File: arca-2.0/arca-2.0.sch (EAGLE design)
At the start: 175 parts, among them IC1 MCP6N11R, IC2 MCP6N11R, IC3 MCP6N11R, IC4 MCP6N11R, IC5 LM324D, IC6 LM324D, SW2 1101M2S3CQE2, T1 FQP30N06L, T2 FQP30N06L, T3 FQP30N06L, T4 FQP30N06L, T5 FQP30N06L, T6 FQP30N06L

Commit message: raspberry pi pinouts
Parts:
- added C28, C29: 0.1u, rcl:C-USC1206
- added CON_TC1, CON_TC2, CON_TC3, CON_TC4: LPTA-4POS, con-phoenix-5mm:LPTA-4POS
- added JP1, JP2, JP3, JP5, JP7: (no value), pinhead:PINHD-1X8
- added JP4, JP6: (no value), pinhead:PINHD-1X4
- added R75, R76: 10k, rcl:R-US_R1206
- added SW1: 1101M2S3CQE2, switch-slide:1101M2S3CQE2
- added X1: 2540-5, con-3m:2540-5
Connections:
- new net ADC1_CS: ADC1.CS*, R76.1, X1-26.KL
- new net ADC2_CS: ADC2.CS*, R74.1, X1-24.KL
- new net ADC3_CS: ADC3.CS*, R75.1, X1-22.KL
- new net N$50: ADC1.CH5, JP1.6
- new net N$51: ADC1.CH6, JP1.7
- new net N$52: ADC1.CH7, JP1.8
- new net N$53: ADC2.CH7, JP2.8
- new net N$54: ADC2.CH6, JP2.7
- new net N$55: ADC2.CH5, JP2.6
- new net N$56: ADC2.CH4, JP2.5
- new net N$57: ADC3.CH4, JP3.5
- new net N$58: ADC3.CH5, JP3.6
- new net N$59: ADC3.CH6, JP3.7
- new net N$60: ADC3.CH7, JP3.8
- new net N$67: JP7.7
- new net N$68: JP7.8
- new net TC1: ADC1.CH0, CON_TC1_2.SK, JP1.1
- new net TC2: ADC1.CH1, CON_TC2_2.SK, JP1.2
- new net TC3: ADC1.CH2, CON_TC3_2.SK, JP1.3
- new net TC4: ADC1.CH3, CON_TC4_2.SK, JP1.4
- net +5V: now also ADC2.VDD, ADC2.VREF, ADC3.VDD, ADC3.VREF, C28.1, C29.1, R74.2, R75.2, R76.2, X1-2.KL, X1-4.KL
- net +5V_FS: now also CON_TC1_1.SK, CON_TC2_1.SK, CON_TC3_1.SK, CON_TC4_1.SK
- net 12V_CON: now also SW1.P
- net 12V_IN: now also SW1.O
- net DRV_CTL_1: now also JP7.1, X1-11.KL
- net DRV_CTL_2: now also JP7.2, X1-13.KL
- net DRV_CTL_3: now also JP7.3, X1-15.KL
- net DRV_CTL_4: now also JP7.4, X1-18.KL
- net DRV_CTL_5: now also JP7.5, X1-33.KL
- net DRV_CTL_6: now also JP7.6, X1-32.KL
- net GND: now also ADC2.AGND, ADC2.DGND, ADC3.AGND, ADC3.DGND, C28.2, C29.2, CON_TC1_4.SK, CON_TC2_4.SK, CON_TC3_4.SK, CON_TC4_4.SK, X1-14.KL, X1-20.KL, X1-25.KL, X1-30.KL, X1-34.KL, X1-39.KL, X1-6.KL, X1-9.KL; no longer R74.1
- net LC1+: now also JP5.1
- net LC1-: now also JP5.2
- net LC1_CAL: now also ADC2.CH0, JP2.1; no longer ADC1.CH0
- net LC1_PREC: now also JP6.1
- net LC2+: now also JP5.3
- net LC2-: now also JP5.4
- net LC2_CAL: now also ADC2.CH1, JP2.2; no longer ADC1.CH1
- net LC2_PREC: now also JP6.2
- net LC3+: now also JP5.5
- net LC3-: now also JP5.6
- net LC3_CAL: now also ADC2.CH2, JP2.3; no longer ADC1.CH2
- net LC3_PREC: now also JP6.3
- net LC4+: now also JP5.7
- net LC4-: now also JP5.8
- net LC4_CAL: now also ADC2.CH3, JP2.4; no longer ADC1.CH3
- net LC4_PREC: now also JP6.4
- net N$49: now also ADC1.CH4, JP1.5; no longer ADC1.CS*, R74.2
- net PT1-: now also JP4.1
- net PT1_CAL: now also ADC3.CH0, JP3.1
- net PT2-: now also JP4.2
- net PT2_CAL: now also ADC3.CH1, JP3.2
- net PT3-: now also JP4.3
- net PT3_CAL: now also ADC3.CH2, JP3.3
- net PT4-: now also JP4.4
- net PT4_CAL: now also ADC3.CH3, JP3.4
- net SPI_CLK: now also ADC2.CLK, ADC3.CLK, X1-23.KL
- net SPI_MISO: now also ADC2.DOUT, ADC3.DOUT, X1-21.KL
- net SPI_MOSI: now also ADC2.DIN, ADC3.DIN, X1-19.KL
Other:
- note added: "Second-order Sallen-Key LPF. f_c = 1/(2 pi sqrt(R55 * R56 * C1 * C2)). G = 1 + (R66/R67)"

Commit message: first rev of board
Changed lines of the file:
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@@
 <attribute name="VALUE" x="119.38" y="124.46" size="1.27" layer="96"/>
 </instance>
-<instance part="SUPPLY1" gate="G$1" x="167.64" y="142.24" smashed="yes">
-<attribute name="VALUE" x="165.1" y="145.415" size="1.778" layer="96"/>
+<instance part="SUPPLY1" gate="G$1" x="165.1" y="142.24" smashed="yes">
+<attribute name="VALUE" x="162.56" y="145.415" size="1.778" layer="96"/>
 </instance>
 <instance part="R1" gate="G$1" x="132.08" y="127" smashed="yes" rot="R90">
@@
 <junction x="144.78" y="134.62"/>
 <pinref part="FS7" gate="G1" pin="2"/>
-<wire x1="144.78" y1="134.62" x2="167.64" y2="134.62" width="0.1524" layer="91"/>
+<wire x1="144.78" y1="134.62" x2="165.1" y2="134.62" width="0.1524" layer="91"/>
 <pinref part="SUPPLY1" gate="G$1" pin="+10V"/>
-<wire x1="167.64" y1="134.62" x2="167.64" y2="139.7" width="0.1524" layer="91"/>
-<junction x="167.64" y="134.62"/>
+<wire x1="165.1" y1="134.62" x2="167.64" y2="134.62" width="0.1524" layer="91"/>
+<wire x1="165.1" y1="139.7" x2="165.1" y2="134.62" width="0.1524" layer="91"/>
 </segment>
 </net>
@@
 </segment>
 </net>
+<net name="N$61" class="5">
+<segment>
+<junction x="165.1" y="134.62"/>
+</segment>
+</net>

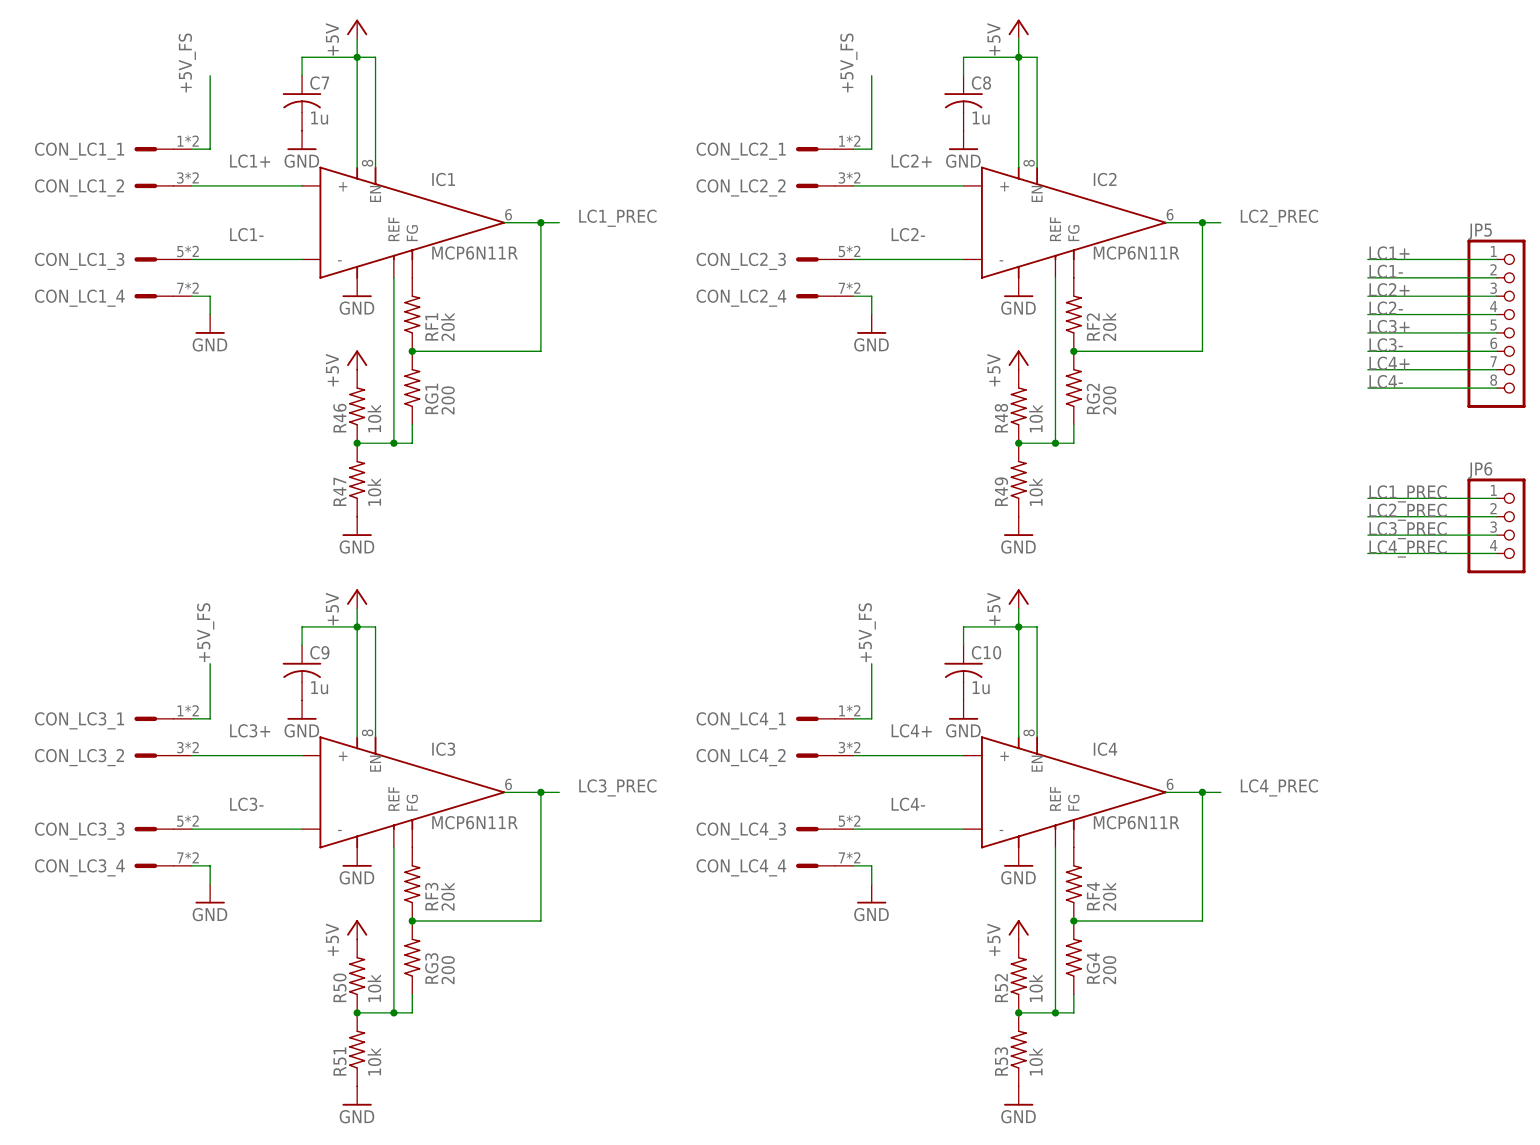
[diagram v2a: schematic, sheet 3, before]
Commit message: resistor cleanup for v_ref
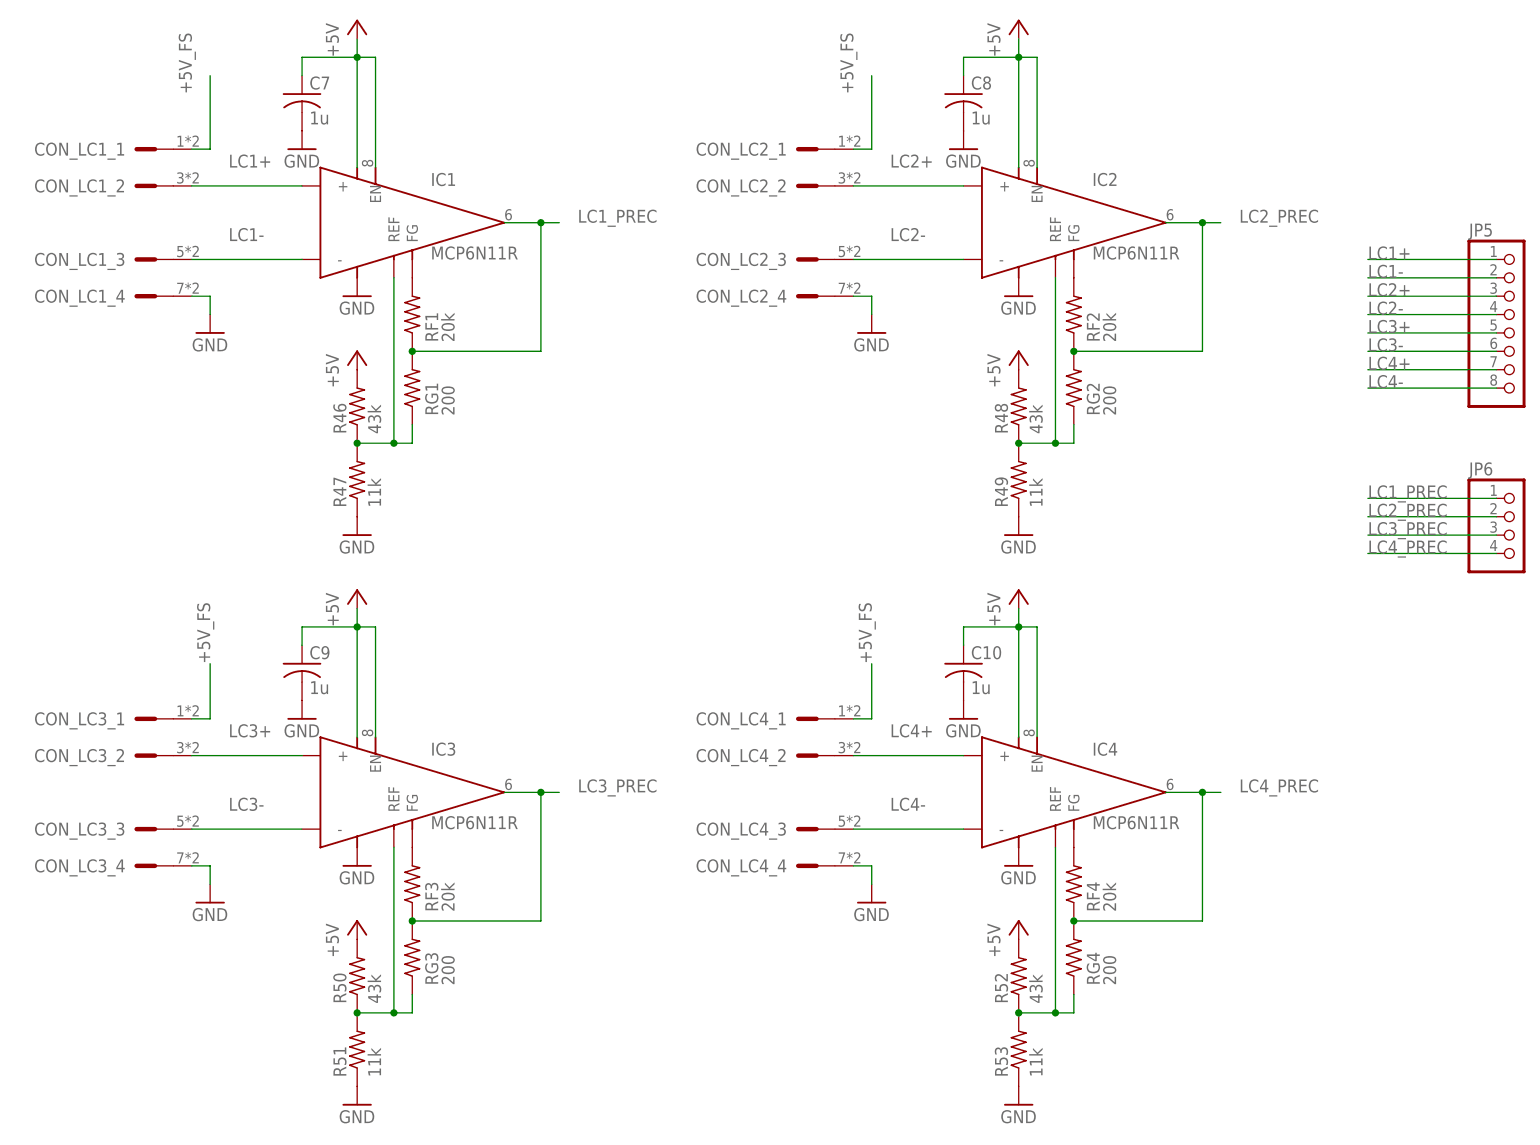
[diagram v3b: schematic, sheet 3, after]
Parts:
- R46, R48, R50, R52: value 10k -> 43k
- R47, R49, R51, R53: value 10k -> 11k
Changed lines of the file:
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@@
 <?xml version="1.0" encoding="utf-8"?>
 <!DOCTYPE eagle SYSTEM "eagle.dtd">
-<eagle version="9.5.0">
+<eagle version="9.6.2">
 <drawing>
 <settings>
@@
 <part name="P+19" library="supply1" library_urn="urn:adsk.eagle:library:371" deviceset="+5V" device=""/>
 <part name="P+20" library="supply1" library_urn="urn:adsk.eagle:library:371" deviceset="+5V" device=""/>
-<part name="R46" library="rcl" library_urn="urn:adsk.eagle:library:334" deviceset="R-US_" device="R1206" package3d_urn="urn:adsk.eagle:package:23540/2" value="10k"/>
-<part name="R47" library="rcl" library_urn="urn:adsk.eagle:library:334" deviceset="R-US_" device="R1206" package3d_urn="urn:adsk.eagle:package:23540/2" value="10k"/>
+<part name="R46" library="rcl" library_urn="urn:adsk.eagle:library:334" deviceset="R-US_" device="R1206" package3d_urn="urn:adsk.eagle:package:23540/2" value="43k"/>
+<part name="R47" library="rcl" library_urn="urn:adsk.eagle:library:334" deviceset="R-US_" device="R1206" package3d_urn="urn:adsk.eagle:package:23540/2" value="11k"/>
 <part name="GND2" library="supply1" library_urn="urn:adsk.eagle:library:371" deviceset="GND" device=""/>
 <part name="P+21" library="supply1" library_urn="urn:adsk.eagle:library:371" deviceset="+5V" device=""/>
-<part name="R48" library="rcl" library_urn="urn:adsk.eagle:library:334" deviceset="R-US_" device="R1206" package3d_urn="urn:adsk.eagle:package:23540/2" value="10k"/>
-<part name="R49" library="rcl" library_urn="urn:adsk.eagle:library:334" deviceset="R-US_" device="R1206" package3d_urn="urn:adsk.eagle:package:23540/2" value="10k"/>
+<part name="R48" library="rcl" library_urn="urn:adsk.eagle:library:334" deviceset="R-US_" device="R1206" package3d_urn="urn:adsk.eagle:package:23540/2" value="43k"/>
+<part name="R49" library="rcl" library_urn="urn:adsk.eagle:library:334" deviceset="R-US_" device="R1206" package3d_urn="urn:adsk.eagle:package:23540/2" value="11k"/>
 <part name="GND4" library="supply1" library_urn="urn:adsk.eagle:library:371" deviceset="GND" device=""/>
 <part name="P+22" library="supply1" library_urn="urn:adsk.eagle:library:371" deviceset="+5V" device=""/>
-<part name="R50" library="rcl" library_urn="urn:adsk.eagle:library:334" deviceset="R-US_" device="R1206" package3d_urn="urn:adsk.eagle:package:23540/2" value="10k"/>
-<part name="R51" library="rcl" library_urn="urn:adsk.eagle:library:334" deviceset="R-US_" device="R1206" package3d_urn="urn:adsk.eagle:package:23540/2" value="10k"/>
+<part name="R50" library="rcl" library_urn="urn:adsk.eagle:library:334" deviceset="R-US_" device="R1206" package3d_urn="urn:adsk.eagle:package:23540/2" value="43k"/>
+<part name="R51" library="rcl" library_urn="urn:adsk.eagle:library:334" deviceset="R-US_" device="R1206" package3d_urn="urn:adsk.eagle:package:23540/2" value="11k"/>
 <part name="GND34" library="supply1" library_urn="urn:adsk.eagle:library:371" deviceset="GND" device=""/>
 <part name="P+23" library="supply1" library_urn="urn:adsk.eagle:library:371" deviceset="+5V" device=""/>
-<part name="R52" library="rcl" library_urn="urn:adsk.eagle:library:334" deviceset="R-US_" device="R1206" package3d_urn="urn:adsk.eagle:package:23540/2" value="10k"/>
-<part name="R53" library="rcl" library_urn="urn:adsk.eagle:library:334" deviceset="R-US_" device="R1206" package3d_urn="urn:adsk.eagle:package:23540/2" value="10k"/>
+<part name="R52" library="rcl" library_urn="urn:adsk.eagle:library:334" deviceset="R-US_" device="R1206" package3d_urn="urn:adsk.eagle:package:23540/2" value="43k"/>
+<part name="R53" library="rcl" library_urn="urn:adsk.eagle:library:334" deviceset="R-US_" device="R1206" package3d_urn="urn:adsk.eagle:package:23540/2" value="11k"/>
 <part name="FS7" library="fuse-holder-littlefuse" deviceset="178.6165" device=""/>
 <part name="FRAME5" library="frames" library_urn="urn:adsk.eagle:library:229" deviceset="LETTER_L" device=""/>
